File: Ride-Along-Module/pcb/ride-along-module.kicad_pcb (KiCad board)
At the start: 2 copper layers, 50.3 x 37.8 mm, 39 parts, among them J1 USB_C_Receptacle_USB2.0_16P, J2 Micro_SD_Card, SW1 SW_DPST, U1 USBLC6-2SC6, U2 STM32U545RETxQ, U3 MS5607-02BA, U4 LSM6DSL

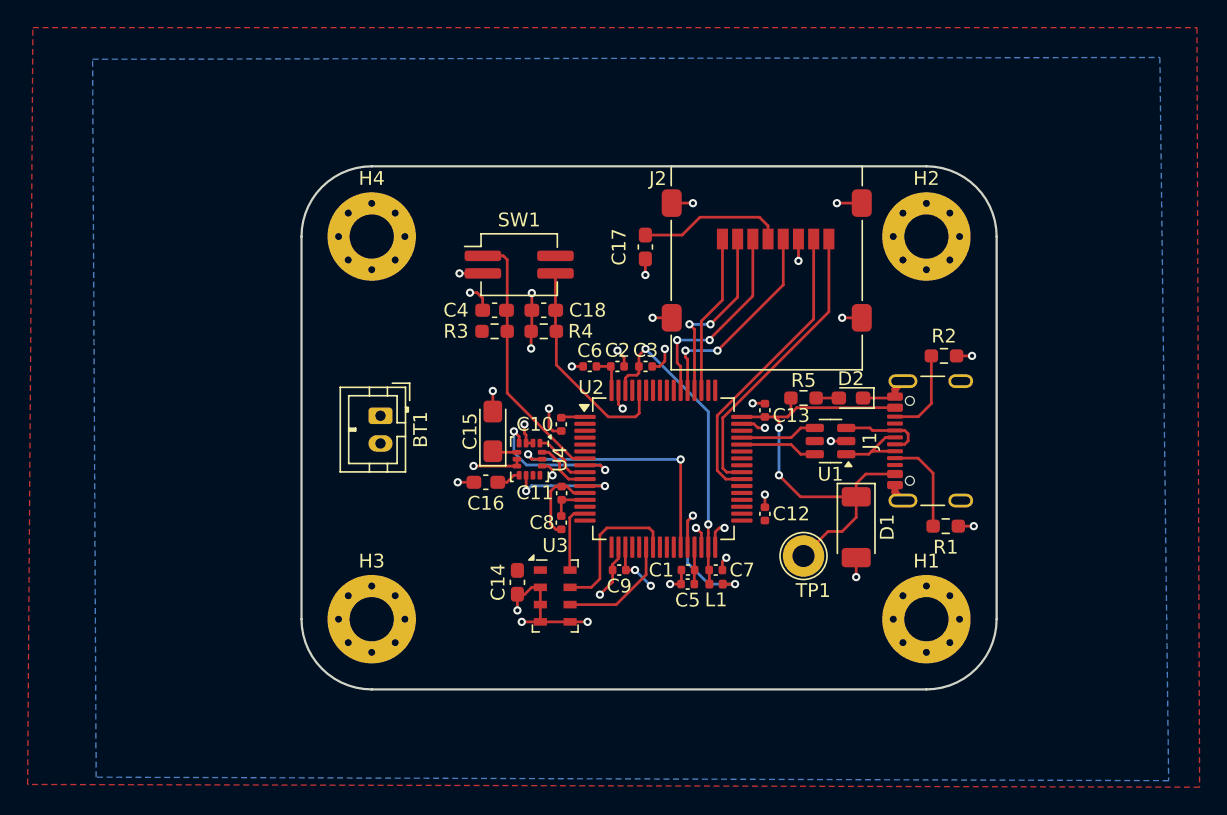
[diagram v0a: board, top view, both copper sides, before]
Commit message: More reuse blocks. Added battery circuit to ride along board
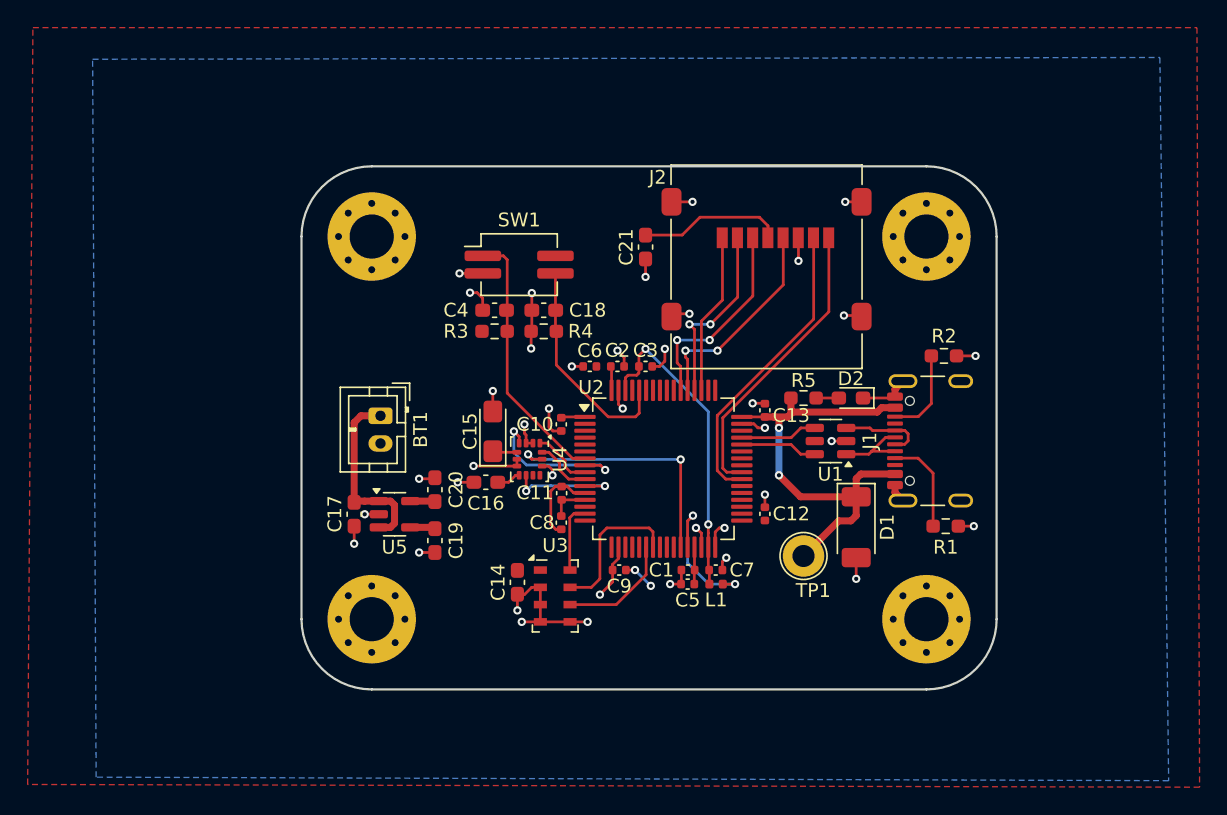
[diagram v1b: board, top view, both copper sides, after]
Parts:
- added C19: 0.01uF, Capacitor_SMD:C_0603_1608Metric_Pad1.08x0.95mm_HandSolder, F.Cu at (125.0, 79.1)
- added C20: 1uF, Capacitor_SMD:C_0603_1608Metric_Pad1.08x0.95mm_HandSolder, F.Cu at (125.0, 75.5)
- added C21: 10u, Capacitor_SMD:C_0603_1608Metric_Pad1.08x0.95mm_HandSolder, F.Cu at (140.2, 57.9)
- added U5: TC2185-3.3VxCTTR, Package_TO_SOT_SMD:SOT-23-5, F.Cu at (122.0, 77.2)
- C17: value 10u -> 1uF
- moved C17 28.6 mm to (119.1, 77.2)
- moved J2 0.09 mm to (149.0, 59.3)
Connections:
- net /IMU/imu_int1 renamed /IMU Sensors/imu_int1
- net /IMU/imu_int2 renamed /IMU Sensors/imu_int2
- net /IMU/imu_miso renamed /IMU Sensors/imu_miso
- net /IMU/imu_mosi renamed /IMU Sensors/imu_mosi
- net /IMU/imu_sclk renamed /IMU Sensors/imu_sclk
- net /IMU/pres_miso renamed /IMU Sensors/pres_miso
- net /IMU/pres_mosi renamed /IMU Sensors/pres_mosi
- net /IMU/pres_sclk renamed /IMU Sensors/pres_sclk
- BT1 pad 1: unconnected-(BT1-+-Pad1) -> Net-(BT1-+)
- BT1 pad 2: unconnected-(BT1---Pad2) -> GNDD
- C17 pad 1: +3V0 -> Net-(BT1-+)
- J2 pad 4: +3V0 -> +3.3V
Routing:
- net Net-(BT1-+): track 0.00 -> 13.5 mm
- net +3V0: track 10.6 -> 0.00 mm
- net +3.3V: track 10.3 -> 20.0 mm
- net GNDD: track 68.0 -> 72.5 mm, vias 35 -> 39
- net Net-(U5-BP): track 0.00 -> 1.82 mm
- net /MCU/VDDUSB: track 34.0 -> 33.4 mm

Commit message: Ride-Along Module Rev. 1
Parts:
- removed the C15 at (129.2, 71.2)
- removed the C16 at (128.7, 74.9)
- removed the C18 at (132.8, 62.5)
- removed the U3 at (133.7, 83.2)
- added C19: 100nF, Capacitor_SMD:C_0603_1608Metric, F.Cu at (131.1, 82.2)
- added C20: 10uF, Capacitor_Tantalum_SMD:CP_EIA-3216-18_Kemet-A, F.Cu at (129.2, 71.0)
- added C21: 100nF, Capacitor_SMD:C_0603_1608Metric, F.Cu at (128.6, 74.9)
- added D3: LED, LED_SMD:LED_0603_1608Metric, F.Cu at (125.7, 66.8)
- added FID1: Fiducial, Fiducial:Fiducial_1mm_Mask3mm, F.Cu at (124.1, 61.5)
- added FID2: Fiducial, Fiducial:Fiducial_1mm_Mask3mm, F.Cu at (127.4, 84.5)
- added FID3: Fiducial, Fiducial:Fiducial_1mm_Mask3mm, F.Cu at (158.6, 62.1)
- added G***: LOGO, LOGO, B.Cu at (140.0, 71.8)
- added JP1: SolderJumper_2_Open, Jumper:SolderJumper-2_P1.3mm_Open_RoundedPad1.0x1.5mm, F.Cu at (129.5, 78.0)
- added R6: 1k, Resistor_SMD:R_0603_1608Metric, F.Cu at (125.7, 70.3)
- added TP2: TestPoint, TestPoint:TestPoint_Loop_D2.60mm_Drill1.6mm_Beaded, F.Cu at (153.8, 84.3)
- added TP3: TestPoint, TestPoint:TestPoint_Loop_D2.60mm_Drill1.6mm_Beaded, F.Cu at (149.6, 84.3)
- added TP4: TestPoint, TestPoint:TestPoint_Loop_D2.60mm_Drill1.6mm_Beaded, F.Cu at (121.0, 64.4)
- added U5: LSM6DSL, Package_LGA:LGA-14_3x2.5mm_P0.5mm_LayoutBorder3x4y, F.Cu at (131.8, 73.3)
- BT1: value Battery_Cell -> LiPo Connector
- C14, C4: footprint Capacitor_SMD:C_0603_1608Metric_Pad1.08x0.95mm_HandSolder -> Capacitor_SMD:C_0603_1608Metric
- C15: renamed from C21; footprint Capacitor_SMD:C_0603_1608Metric_Pad1.08x0.95mm_HandSolder -> Capacitor_SMD:C_0603_1608Metric
- C16: renamed from C17; footprint Capacitor_SMD:C_0603_1608Metric_Pad1.08x0.95mm_HandSolder -> Capacitor_SMD:C_0603_1608Metric
- C17: renamed from C19; footprint Capacitor_SMD:C_0603_1608Metric_Pad1.08x0.95mm_HandSolder -> Capacitor_SMD:C_0603_1608Metric
- C18: renamed from C20; footprint Capacitor_SMD:C_0603_1608Metric_Pad1.08x0.95mm_HandSolder -> Capacitor_SMD:C_0603_1608Metric
- D1: renamed from D2; footprint LED_SMD:LED_0603_1608Metric_Pad1.05x0.95mm_HandSolder -> LED_SMD:LED_0603_1608Metric
- R1: renamed from R5; footprint Resistor_SMD:R_0603_1608Metric_Pad0.98x0.95mm_HandSolder -> Resistor_SMD:R_0603_1608Metric
- R2: renamed from R1; footprint Resistor_SMD:R_0603_1608Metric_Pad0.98x0.95mm_HandSolder -> Resistor_SMD:R_0603_1608Metric
- R3: renamed from R2; footprint Resistor_SMD:R_0603_1608Metric_Pad0.98x0.95mm_HandSolder -> Resistor_SMD:R_0603_1608Metric
- R4: renamed from R3; footprint Resistor_SMD:R_0603_1608Metric_Pad0.98x0.95mm_HandSolder -> Resistor_SMD:R_0603_1608Metric
- R5: renamed from R4; footprint Resistor_SMD:R_0603_1608Metric_Pad0.98x0.95mm_HandSolder -> Resistor_SMD:R_0603_1608Metric
- SW1: footprint Button_Switch_SMD:SW_DIP_SPSTx02_Slide_KingTek_DSHP02TJ_W5.25mm_P1.27mm_JPin -> Button_Switch_SMD:SW_DIP_SPSTx02_Slide_Copal_CHS-02A_W5.08mm_P1.27mm_JPin
- U4: value LSM6DSL -> MS5607-02BA; footprint Package_LGA:LGA-14_3x2.5mm_P0.5mm_LayoutBorder3x4y -> Package_LGA:LGA-8_3x5mm_P1.25mm
- moved C14 19.7 mm to (132.9, 62.5), turned to 0 degrees
- moved U4 10.1 mm to (133.7, 83.2), turned to 0 degrees
- moved D2 3.38 mm to (153.7, 75.3), turned to 180 degrees
- moved C16 2.74 mm to (121.8, 76.6)
- moved U3 2.58 mm to (124.6, 76.8)
- moved R2 2.29 mm to (159.6, 78.1), turned to 180 degrees
- moved TP1 2.16 mm to (153.8, 80.1)
- moved R3 2.16 mm to (159.6, 65.8), turned to 180 degrees
- moved C18 2.08 mm to (125.7, 73.5)
- moved C17 1.15 mm to (125.7, 80.0)
- moved C9 0.38 mm to (138.7, 81.3)
- moved R4 0.18 mm to (129.4, 64.1)
- moved C10 0.16 mm to (134.1, 70.6)
- moved C4 0.13 mm to (129.4, 62.5)
- moved R5 0.11 mm to (132.9, 64.1)
- renumbered D1 to D2, U5 to U3
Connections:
- net Net-(BT1-+) renamed /3v7 LiPo to 3v3 Supply/V_BAT
- C14 pad 1: +3.3V -> GNDD
- C14 pad 2: GNDD -> /MCU/BOOT0
- U2 pad 17: unconnected-(U2-PA3-Pad17) -> /IMU Sensors/pres_cs
- U2 pad 6: unconnected-(U2-PH1-Pad6) -> /IMU Sensors/imu_cs
- U4 pad 1: /IMU Sensors/imu_mosi -> +3.3V
- U4 pad 4: /IMU Sensors/imu_int1 -> /IMU Sensors/pres_cs
- U4 pad 5: +3.3V -> /IMU Sensors/pres_cs
- U4 pad 6: GNDD -> /IMU Sensors/pres_miso
- U4 pad 7: GNDD -> /IMU Sensors/pres_mosi
- U4 pad 8: +3.3V -> /IMU Sensors/pres_sclk
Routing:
- net /IMU Sensors/pres_cs: track 0.00 -> 9.57 mm, vias 0 -> 2
- net /IMU Sensors/imu_cs: track 0.00 -> 9.06 mm, vias 0 -> 2
- net GNDD: track 72.5 -> 64.9 mm, vias 39 -> 35
- net /3v7 LiPo to 3v3 Supply/V_BAT: track 13.5 -> 20.0 mm
- net +3.3V: track 20.0 -> 14.4 mm, vias 2 -> 0
- net /MCU/VDDUSB: track 33.4 -> 28.7 mm, vias 2 -> 0
- net GNDA: track 6.12 -> 9.17 mm
- net Net-(D3-A): track 0.00 -> 1.66 mm
- net Net-(J1-CC1): track 7.04 -> 6.44 mm, vias 0 -> 2
- net Net-(J1-CC2): track 6.47 -> 6.66 mm, vias 0 -> 2
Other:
- board text added: "Ride-Along Module Rev. 1"
